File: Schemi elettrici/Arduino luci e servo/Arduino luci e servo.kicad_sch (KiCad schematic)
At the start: 21 parts, among them M1 Motor_Servo, M2 Motor_Servo, M3 Motor_Servo, M4 Motor_Servo, M5 Motor_Servo, M6 Motor_Servo, M7 Motor_Servo, M8 Motor_Servo

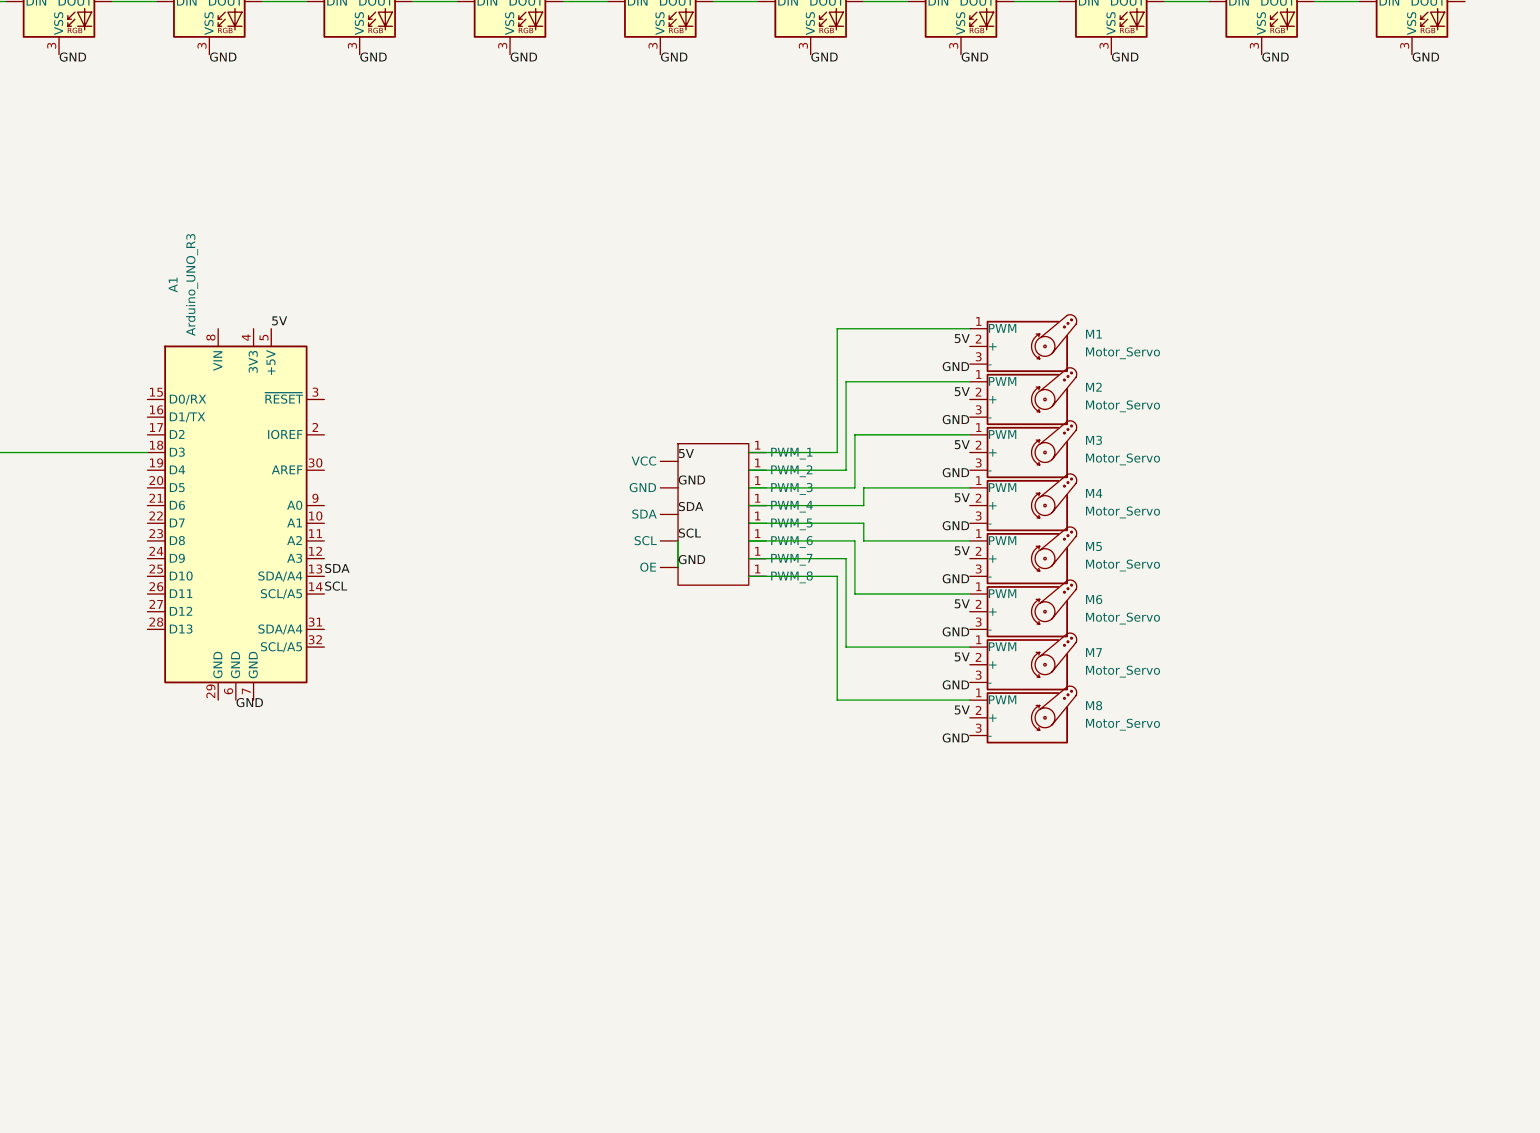
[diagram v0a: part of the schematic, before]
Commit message: Aggiunto tutto il coso del relè
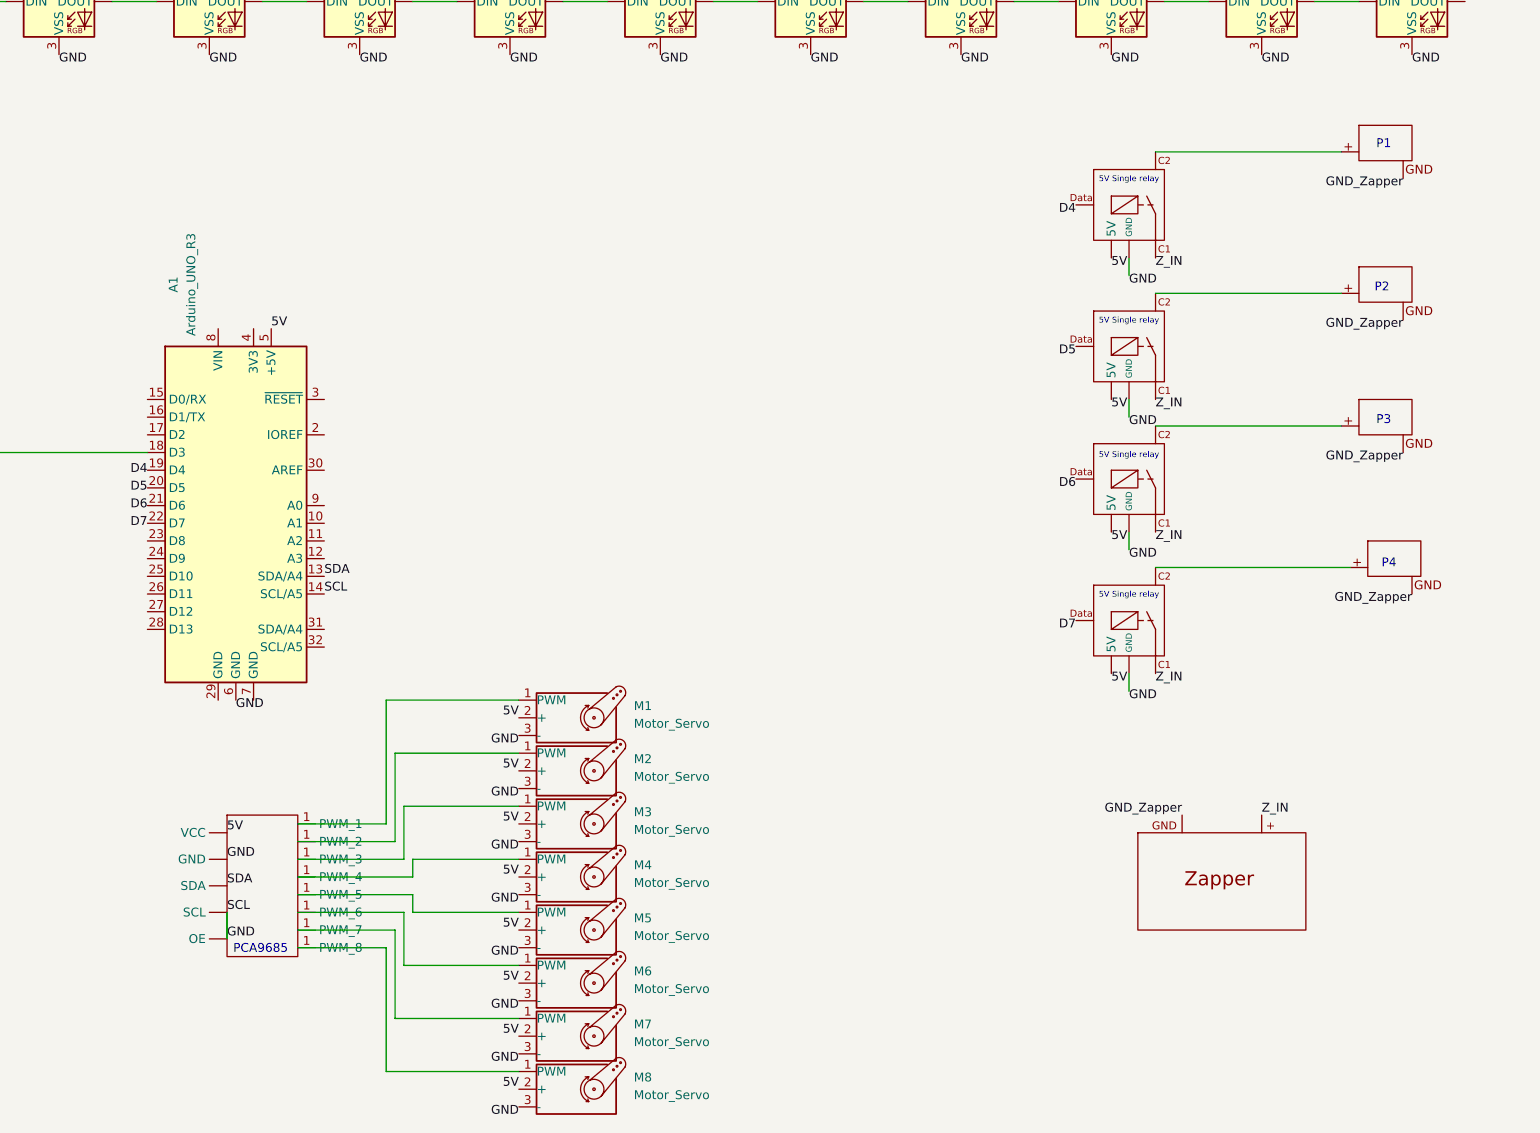
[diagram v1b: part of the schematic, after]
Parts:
- added U10, U7, U8, U9: ~, symbol relè:Player
- added U2, U3, U4, U5: ~, symbol relè:relè
- added U6: ~, symbol relè:zapper
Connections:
- net 5V: now also U2., U3., U4., U5.
- net GND: now also U2., U3., U4., U5.
- net D4: now reaches A1.19 (D4)
- net D4: now also U2.
- net D5: now reaches A1.20 (D5)
- net D5: now also U3.
- net D6: now reaches A1.21 (D6)
- net D6: now also U4.
- net D7: now reaches A1.22 (D7)
- net D7: now also U5.
- new net: U4., U9.
- new net: U3., U8.
- new net: U10., U5.
- new net: U2., U7.
- new net GND_Zapper: U10., U6., U7., U8., U9.
- new net Z_IN: U2., U3., U4., U5., U6.
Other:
- note added: "5V Single relay"
- note added: "P1"
- note added: "P2"
- note added: "P3"
- note added: "P4"
- note added: "PCA9685"
- moved on the sheet: M1, M2, M3, M4, M5, M6, M7, M8

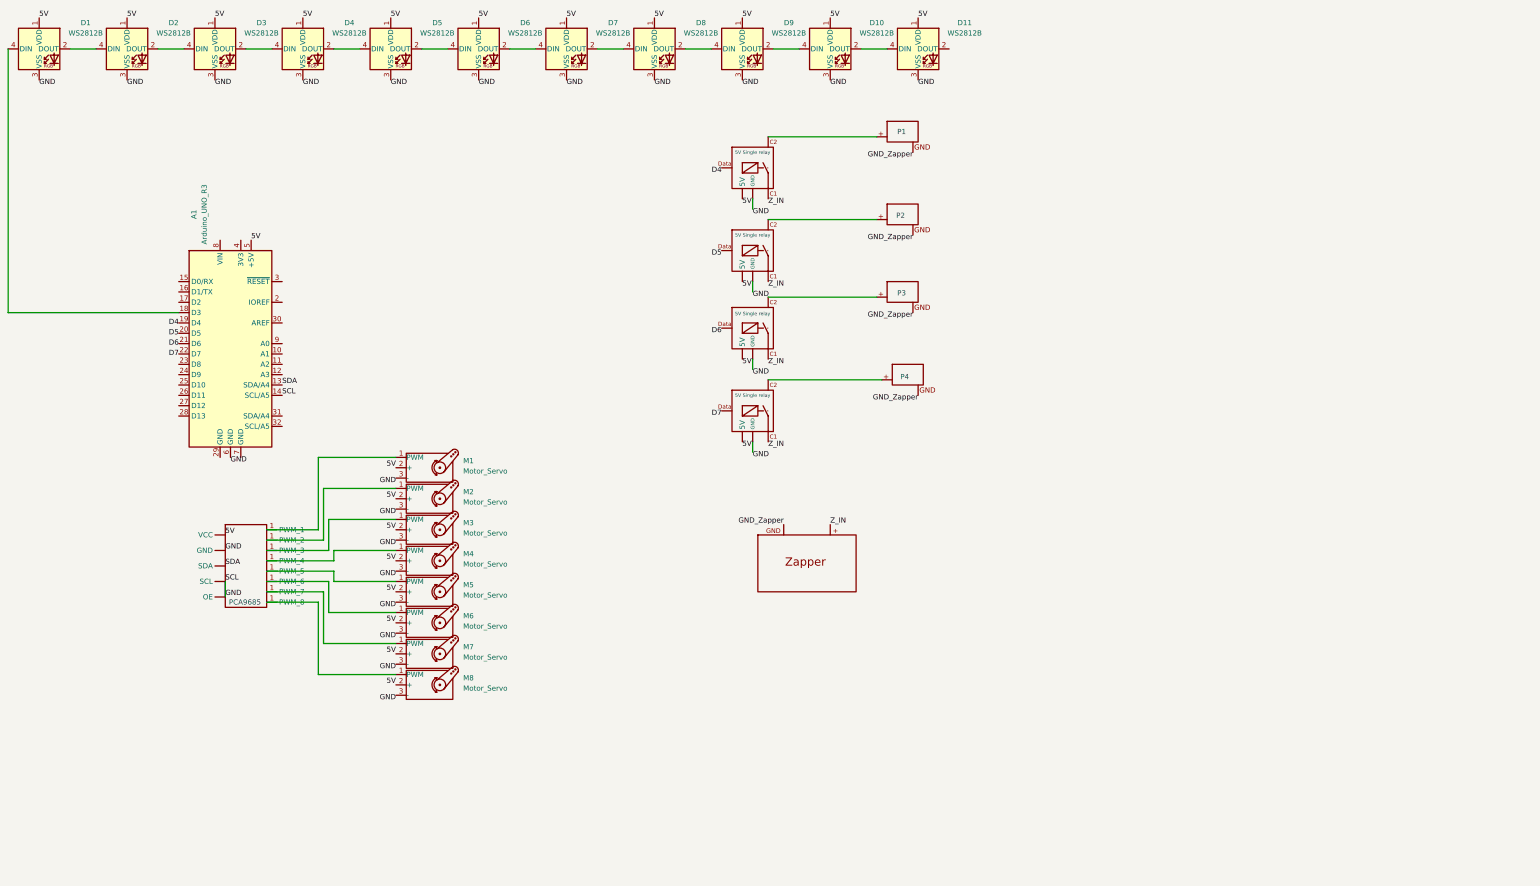
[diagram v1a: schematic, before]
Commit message: Aggiunte le altre 3 strisce led allo schema Arduino e creato lo schema per l'ESP
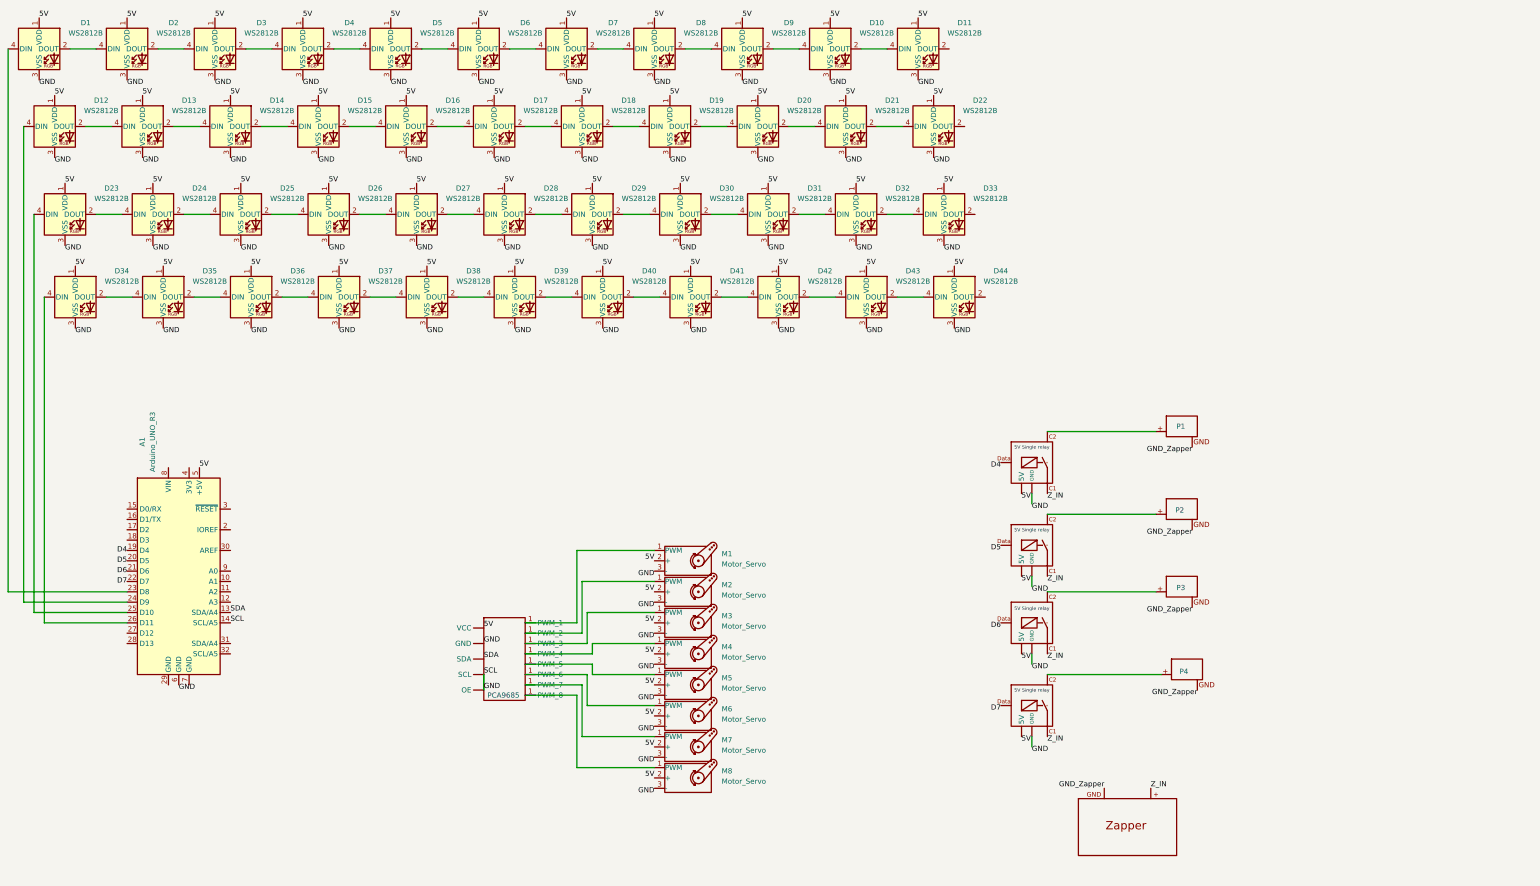
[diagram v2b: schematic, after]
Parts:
- added D12, D13, D14, D15, D16, D17, D18, D19, D20, D21, D22, D23, D24, D25, D26, D27, D28, D29, D30, D31, D32, D33, D34, D35, D36, D37, D38, D39, D40, D41, D42, D43, D44: WS2812B, LED_SMD:LED_WS2812B_PLCC4_5.0x5.0mm_P3.2mm, symbol LED:WS2812B
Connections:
- net 5V: now also D12.1 (VDD), D13.1 (VDD), D14.1 (VDD), D15.1 (VDD), D16.1 (VDD), D17.1 (VDD), D18.1 (VDD), D19.1 (VDD), D20.1 (VDD), D21.1 (VDD), D22.1 (VDD), D23.1 (VDD), D24.1 (VDD), D25.1 (VDD), D26.1 (VDD), D27.1 (VDD), D28.1 (VDD), D29.1 (VDD), D30.1 (VDD), D31.1 (VDD), D32.1 (VDD), D33.1 (VDD), D34.1 (VDD), D35.1 (VDD), D36.1 (VDD), D37.1 (VDD), D38.1 (VDD), D39.1 (VDD), D40.1 (VDD), D41.1 (VDD), D42.1 (VDD), D43.1 (VDD), D44.1 (VDD)
- net GND: now also D12.3 (VSS), D13.3 (VSS), D14.3 (VSS), D15.3 (VSS), D16.3 (VSS), D17.3 (VSS), D18.3 (VSS), D19.3 (VSS), D20.3 (VSS), D21.3 (VSS), D22.3 (VSS), D23.3 (VSS), D24.3 (VSS), D25.3 (VSS), D26.3 (VSS), D27.3 (VSS), D28.3 (VSS), D29.3 (VSS), D30.3 (VSS), D31.3 (VSS), D32.3 (VSS), D33.3 (VSS), D34.3 (VSS), D35.3 (VSS), D36.3 (VSS), D37.3 (VSS), D38.3 (VSS), D39.3 (VSS), D40.3 (VSS), D41.3 (VSS), D42.3 (VSS), D43.3 (VSS), D44.3 (VSS)
- net at D1.4 (DIN): now also A1.23 (D8); no longer A1.18 (D3)
- net at A1.24 (D9): now also D12.4 (DIN)
- net at A1.25 (D10): now also D23.4 (DIN)
- net at A1.26 (D11): now also D34.4 (DIN)
- new net: D25.2 (DOUT), D26.4 (DIN)
- new net: D24.2 (DOUT), D25.4 (DIN)
- new net: D12.2 (DOUT), D13.4 (DIN)
- new net: D21.2 (DOUT), D22.4 (DIN)
- new net: D18.2 (DOUT), D19.4 (DIN)
- new net: D17.2 (DOUT), D18.4 (DIN)
- new net: D43.2 (DOUT), D44.4 (DIN)
- new net: D42.2 (DOUT), D43.4 (DIN)
- new net: D15.2 (DOUT), D16.4 (DIN)
- new net: D14.2 (DOUT), D15.4 (DIN)
- new net: D38.2 (DOUT), D39.4 (DIN)
- new net: D37.2 (DOUT), D38.4 (DIN)
- new net: D27.2 (DOUT), D28.4 (DIN)
- new net: D26.2 (DOUT), D27.4 (DIN)
- new net: D28.2 (DOUT), D29.4 (DIN)
- new net: D30.2 (DOUT), D31.4 (DIN)
- new net: D29.2 (DOUT), D30.4 (DIN)
- new net: D36.2 (DOUT), D37.4 (DIN)
- new net: U4., U9.
- new net: U3., U8.
- new net: D19.2 (DOUT), D20.4 (DIN)
- new net: D39.2 (DOUT), D40.4 (DIN)
- new net: D40.2 (DOUT), D41.4 (DIN)
- new net: D35.2 (DOUT), D36.4 (DIN)
- new net: D34.2 (DOUT), D35.4 (DIN)
- new net: D32.2 (DOUT), D33.4 (DIN)
- new net: D31.2 (DOUT), D32.4 (DIN)
- new net: D23.2 (DOUT), D24.4 (DIN)
- new net: D20.2 (DOUT), D21.4 (DIN)
- new net: D13.2 (DOUT), D14.4 (DIN)
- new net: U10., U5.
- new net: D16.2 (DOUT), D17.4 (DIN)
- new net: D41.2 (DOUT), D42.4 (DIN)
- new net: U2., U7.
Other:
- moved on the sheet: A1, M1, M2, M3, M4, M5, M6, M7, M8

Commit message: Messi gli schemi in foglio orizzontale che mi piacciono di più :)
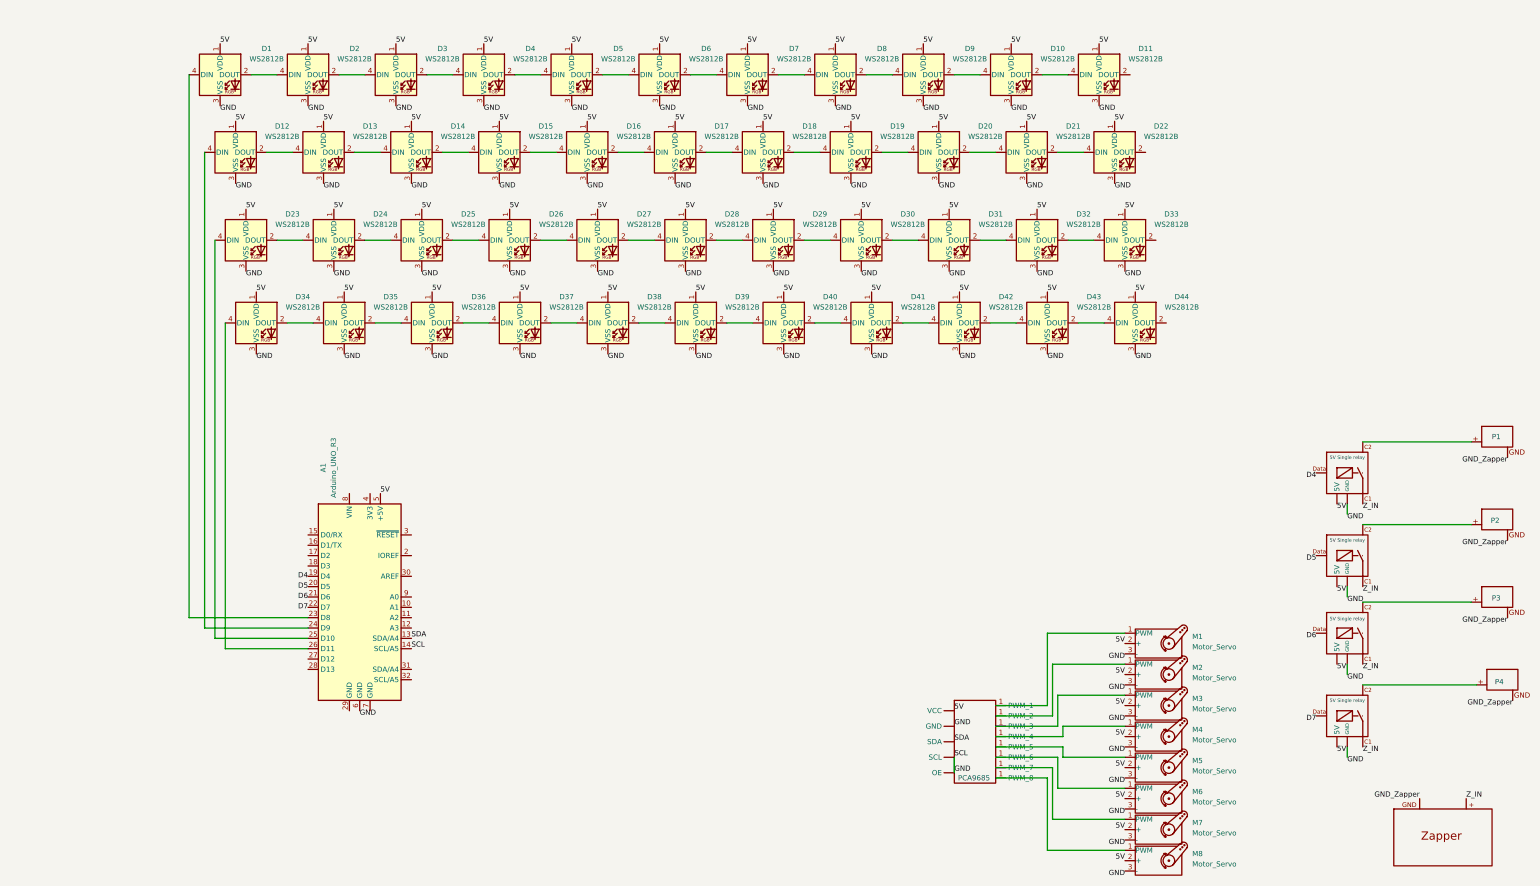
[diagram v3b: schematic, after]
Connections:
- new net: U4., U9.
- new net: U3., U8.
- new net: U10., U5.
- new net: U2., U7.
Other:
- moved on the sheet: A1, D1, D10, D11, D12, D13, D14, D15, D16, D17, D18, D19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

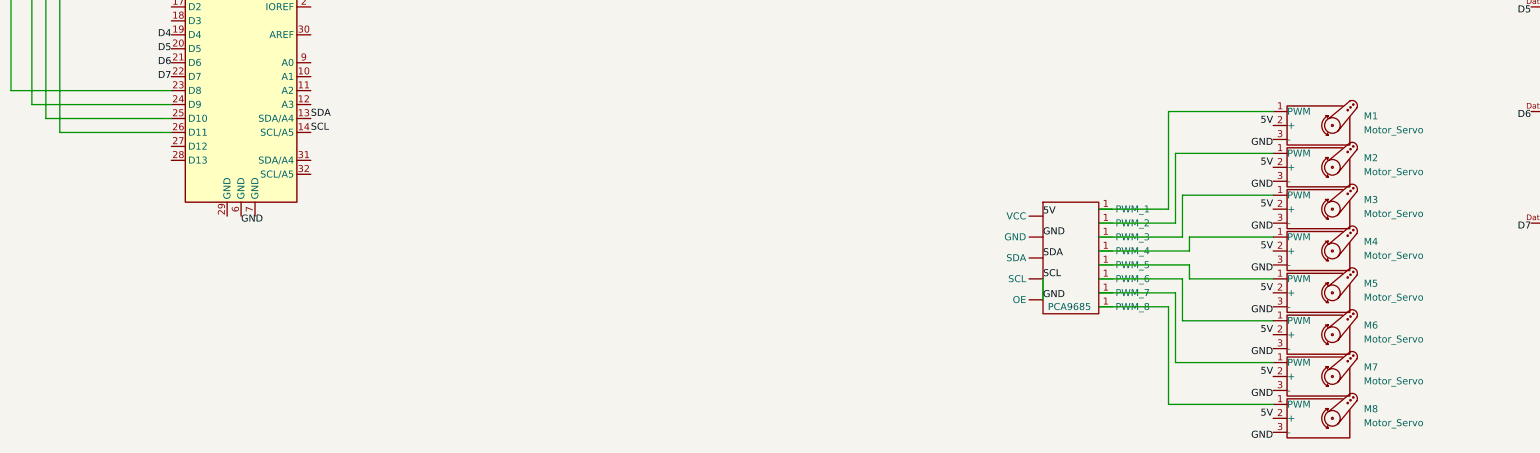
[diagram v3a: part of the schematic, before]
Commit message: Modificato schema arduino: messi led shell
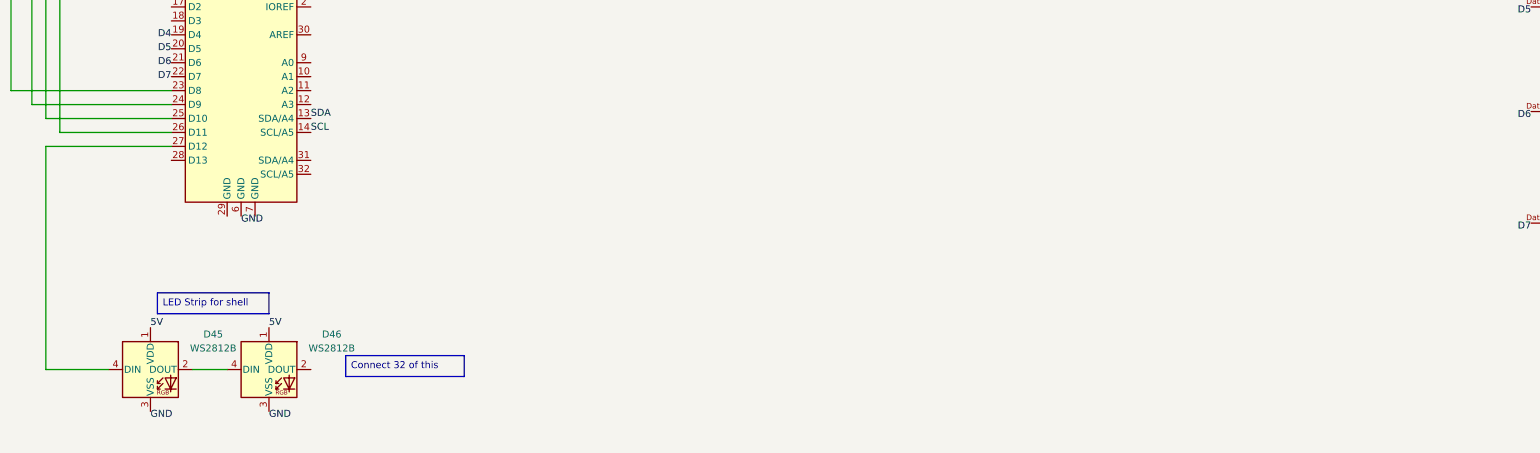
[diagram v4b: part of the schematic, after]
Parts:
- removed M1, M2, M3, M4, M5, M6, M7, M8: Motor_Servo, symbol Motor:Motor_Servo
- removed U1: ~, symbol PCA9685kicad_sym:PCA9685_Breakout
- added D45, D46: WS2812B, LED_SMD:LED_WS2812B_PLCC4_5.0x5.0mm_P3.2mm, symbol LED:WS2812B
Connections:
- net 5V: now also D45.1 (VDD), D46.1 (VDD)
- net GND: now also D45.3 (VSS), D46.3 (VSS); no longer A1.14 (SCL/A5)
- net at A1.27 (D12): now also D45.4 (DIN)
- new net: U4., U9.
- new net: U3., U8.
- new net: D45.2 (DOUT), D46.4 (DIN)
- new net: U10., U5.
- new net: U2., U7.
- new net SCL: A1.14 (SCL/A5)
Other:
- note removed: "PCA9685"
